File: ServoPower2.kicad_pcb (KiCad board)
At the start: 2 copper layers, 26 x 57.2 mm, 16 parts, among them J1 Conn_01x03, J10 Conn_01x03, J11 Conn_01x03, J12 Conn_01x03, J13 Conn_01x02, J14 Conn_01x02, J15 Conn_01x02, J2 Conn_01x03, J3 Conn_01x03, J4 Conn_01x03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

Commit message: pdb
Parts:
- removed pi1: pi, Connector_PinSocket_2.54mm:PinSocket_2x20_P2.54mm_Vertical
- added U1: Teensy4.0, teensy:Teensy40, F.Cu at (143.5, 82.5)
- moved J12 5.24 mm to (157.5, 104.1)
- moved J11 4.02 mm to (157.5, 101.6)
- moved J9 4.02 mm to (157.5, 94.0)
- moved J6 2.84 mm to (157.5, 83.8)
- moved J8 2.84 mm to (157.5, 91.4)
- moved J10 2.84 mm to (157.5, 99.1)
- moved J3 1.80 mm to (157.5, 73.7)
- moved J1 1.80 mm to (157.5, 68.6)
- moved J5 1.80 mm to (157.5, 81.3)
- moved J7 1.80 mm to (157.5, 88.9)
- moved J14 1.27 mm to (152.4, 63.5)
- moved J13 1.27 mm to (157.5, 114.3)
- moved J2 1.27 mm to (157.5, 71.1)
- moved J4 1.27 mm to (157.5, 78.7)
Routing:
- net +5V: track 4.86 -> 18.6 mm
- net /S41: track 23.8 -> 11.0 mm
- net /S33: track 19.0 -> 9.94 mm
- net /S43: track 24.2 -> 32.0 mm
- net /S32: track 16.6 -> 9.94 mm
- net /S31: track 17.1 -> 10.6 mm
- net /S22: track 13.5 -> 8.89 mm
- net /S21: track 13.0 -> 8.89 mm
- net /S23: track 11.5 -> 8.89 mm
- net /S13: track 8.89 -> 10.6 mm
- net /S42: track 26.2 -> 25.2 mm
- net /S12: track 9.42 -> 9.94 mm
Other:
- board size 26 x 57.2 mm -> 40.6 x 57.8 mm
- net class Power: trace_width 1 -> 0.8
- board text added: "Pupper PDB v0.3 Feb ‘20"
- board text removed: "Pupper PDB v0.2 Oct ‘19"

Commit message: clean up
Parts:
- J13: footprint Connector_AMASS:AMASS_XT30U-M_1x02_P5.0mm_Vertical -> Connector_AMASS:AMASS_XT60-M_1x02_P7.20mm_Vertical
- moved U1 29.3 mm to (172.7, 85.1)
- moved J13 5.12 mm to (161.9, 111.8)
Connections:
- U1 pad 1: Net-(U1-Pad1) -> GND
- U1 pad 12: Net-(U1-Pad12) -> (no net)
- U1 pad 13: Net-(U1-Pad13) -> (no net)
- U1 pad 14: Net-(U1-Pad14) -> (no net)
- U1 pad 15: Net-(U1-Pad15) -> (no net)
- U1 pad 16: Net-(U1-Pad16) -> (no net)
- U1 pad 17: Net-(U1-Pad17) -> GND
- U1 pad 18: Net-(U1-Pad18) -> (no net)
- U1 pad 19: Net-(U1-Pad19) -> (no net)
- U1 pad 20: Net-(U1-Pad20) -> (no net)
- U1 pad 23: Net-(U1-Pad23) -> (no net)
- U1 pad 24: Net-(U1-Pad24) -> (no net)
- U1 pad 25: Net-(U1-Pad25) -> (no net)
- U1 pad 26: Net-(U1-Pad26) -> (no net)
- U1 pad 27: Net-(U1-Pad27) -> (no net)
- U1 pad 28: Net-(U1-Pad28) -> (no net)
- U1 pad 29: Net-(U1-Pad29) -> (no net)
- U1 pad 30: Net-(U1-Pad30) -> (no net)
- U1 pad 31: Net-(U1-Pad31) -> (no net)
- U1 pad 34: Net-(U1-Pad34) -> (no net)
- U1 pad 35: Net-(U1-Pad35) -> (no net)
- U1 pad 36: Net-(U1-Pad36) -> (no net)
- U1 pad 37: Net-(U1-Pad37) -> (no net)
- U1 pad 38: Net-(U1-Pad38) -> (no net)
- U1 pad 39: Net-(U1-Pad39) -> (no net)
- U1 pad 40: Net-(U1-Pad40) -> (no net)
- U1 pad 41: Net-(U1-Pad41) -> (no net)
- U1 pad 42: Net-(U1-Pad42) -> (no net)
- U1 pad 43: Net-(U1-Pad43) -> (no net)
- U1 pad 44: Net-(U1-Pad44) -> (no net)
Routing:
- net /S31: track 10.6 -> 8.67 mm
- net /S13: track 10.6 -> 8.67 mm
- net /S43: track 32.0 -> 30.7 mm
- net /S33: track 9.94 -> 8.67 mm
- net /S32: track 9.94 -> 8.67 mm
- net /S23: track 8.89 -> 7.62 mm
- net /S22: track 8.89 -> 7.62 mm
- net /S21: track 8.89 -> 7.62 mm
- net +5V: track 18.6 -> 17.3 mm
- net /S11: track 9.94 -> 8.67 mm
- net /S41: track 11.0 -> 9.72 mm
- net /S12: track 9.94 -> 8.81 mm
- net /S42: track 25.2 -> 24.3 mm
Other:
- board text added: "Vbat"
- board text removed: "Unregulated Vbat"

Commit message: pcb
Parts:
- added U2: IMUBN, Sparkfun:IMUBN, F.Cu at (198.1, 85.1)
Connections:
- U1 pad 12: (no net) -> Net-(U1-Pad12)
- U1 pad 13: (no net) -> Net-(U1-Pad13)
- U1 pad 14: (no net) -> Net-(U1-Pad14)
- U1 pad 15: (no net) -> Net-(U1-Pad15)
- U1 pad 16: (no net) -> Net-(U1-Pad16)
- U1 pad 18: (no net) -> Net-(U1-Pad18)
- U1 pad 19: (no net) -> Net-(U1-Pad19)
- U1 pad 20: (no net) -> Net-(U1-Pad20)
- U1 pad 23: (no net) -> Net-(U1-Pad23)
- U1 pad 24: (no net) -> /INT
- U1 pad 25: (no net) -> /SDA
- U1 pad 26: (no net) -> /SCL
- U1 pad 27: (no net) -> Net-(U1-Pad27)
- U1 pad 28: (no net) -> Net-(U1-Pad28)
- U1 pad 29: (no net) -> Net-(U1-Pad29)
- U1 pad 30: (no net) -> Net-(U1-Pad30)
- U1 pad 31: (no net) -> Net-(U1-Pad31)
- U1 pad 34: (no net) -> Net-(U1-Pad34)
- U1 pad 35: (no net) -> Net-(U1-Pad35)
- U1 pad 36: (no net) -> Net-(U1-Pad36)
- U1 pad 37: (no net) -> Net-(U1-Pad37)
- U1 pad 38: (no net) -> Net-(U1-Pad38)
- U1 pad 39: (no net) -> Net-(U1-Pad39)
- U1 pad 40: (no net) -> Net-(U1-Pad40)
- U1 pad 41: (no net) -> Net-(U1-Pad41)
- U1 pad 42: (no net) -> Net-(U1-Pad42)
- U1 pad 43: (no net) -> Net-(U1-Pad43)
- U1 pad 44: (no net) -> Net-(U1-Pad44)
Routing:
- net GND: track 0.00 -> 12.8 mm
- net /SCL: track 0.00 -> 11.4 mm
- net /SDA: track 0.00 -> 7.40 mm
- net /INT: track 0.00 -> 7.40 mm
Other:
- board size 40.6 x 57.8 mm -> 67.9 x 57.8 mm

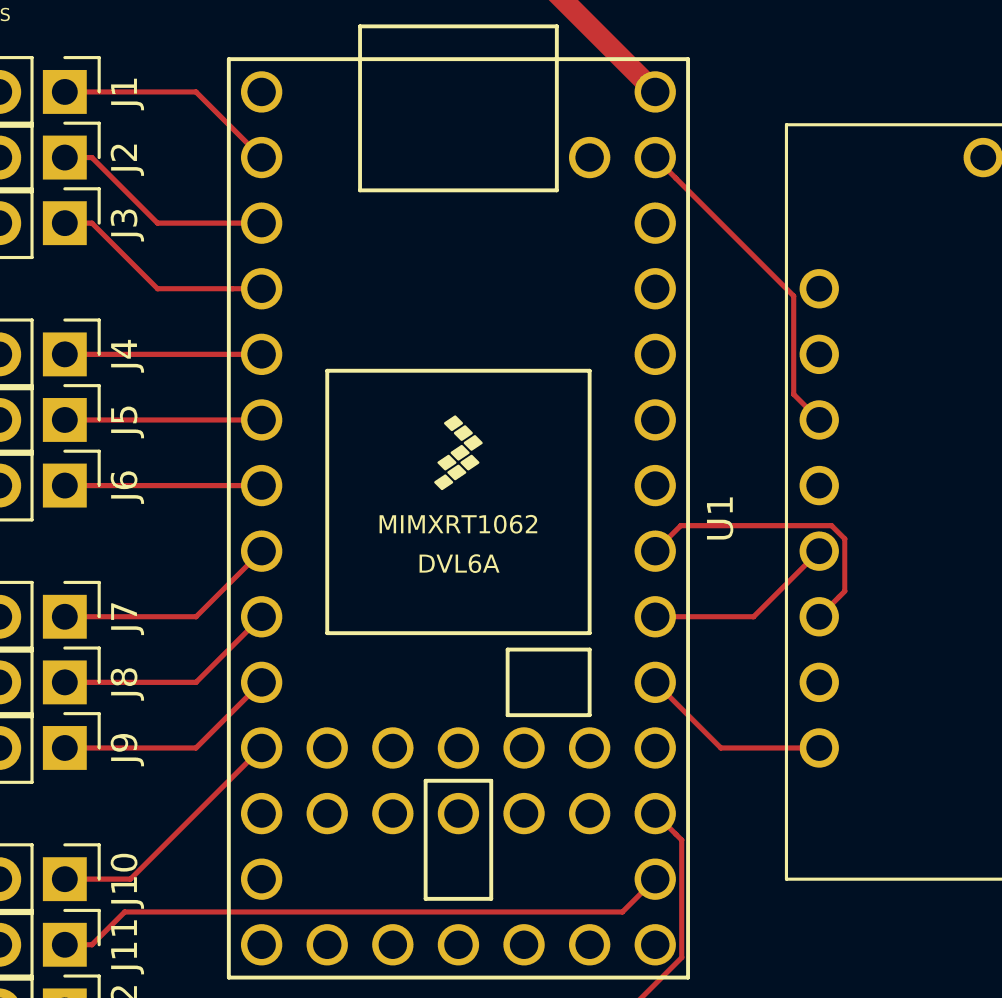
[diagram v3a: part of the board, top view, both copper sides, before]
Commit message: added 3v3
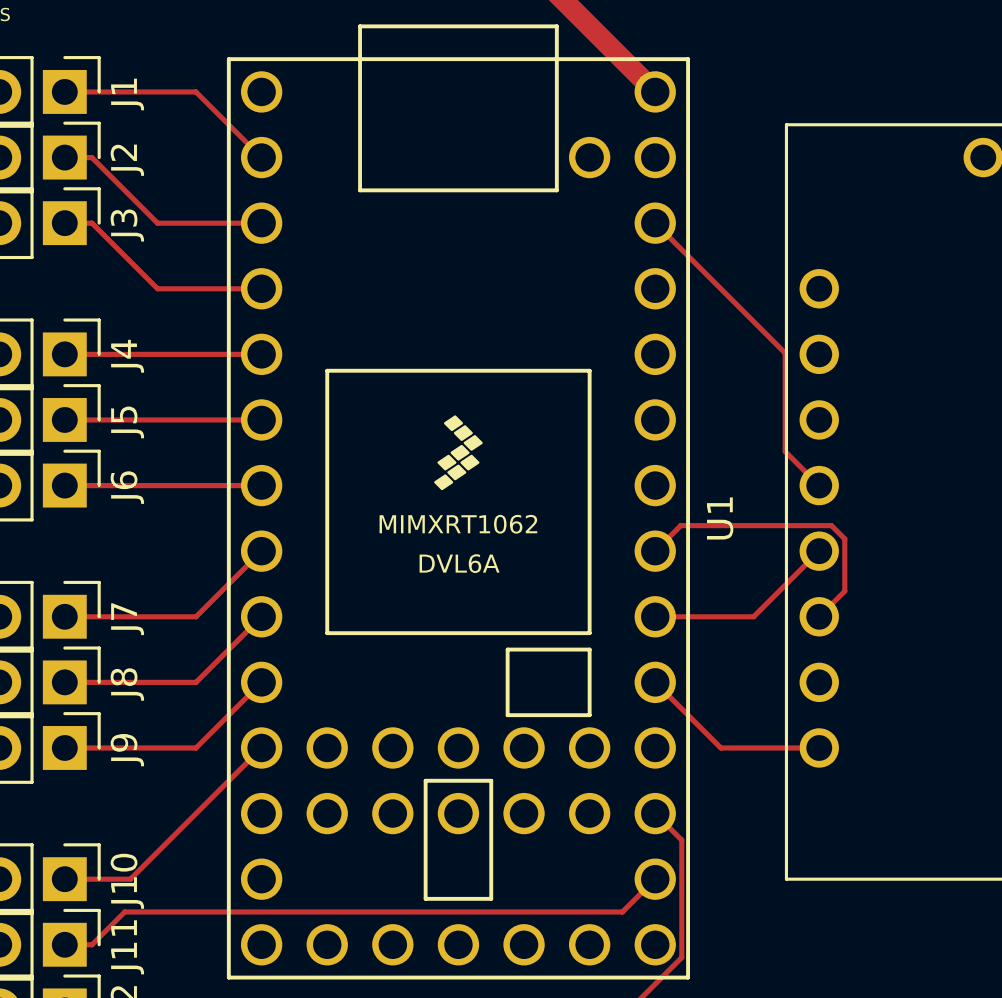
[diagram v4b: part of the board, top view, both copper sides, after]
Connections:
- U1 pad 31: Net-(U1-Pad31) -> +3V3
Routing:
- net +3V3: track 0.00 -> 12.8 mm
- net GND: track 12.8 -> 0.00 mm

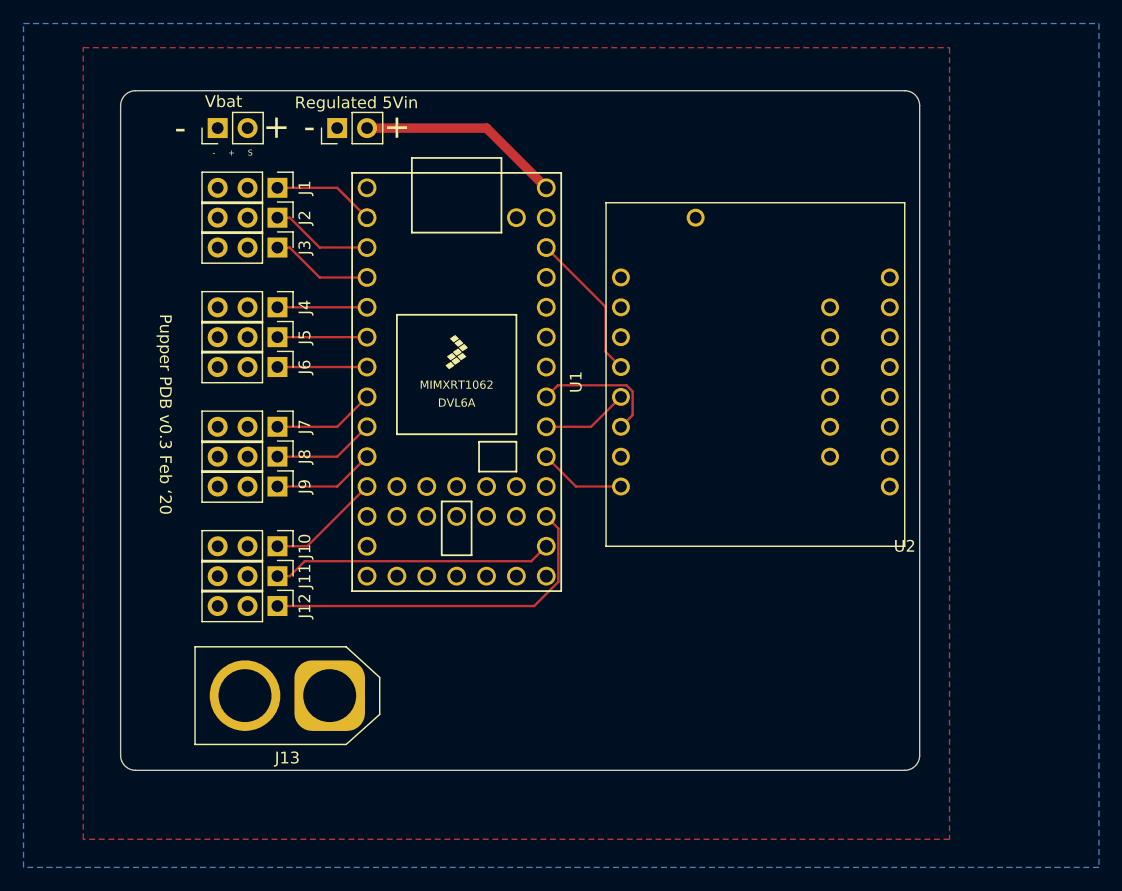
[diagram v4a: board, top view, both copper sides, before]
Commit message: added local dependency to imu symbol and footprint
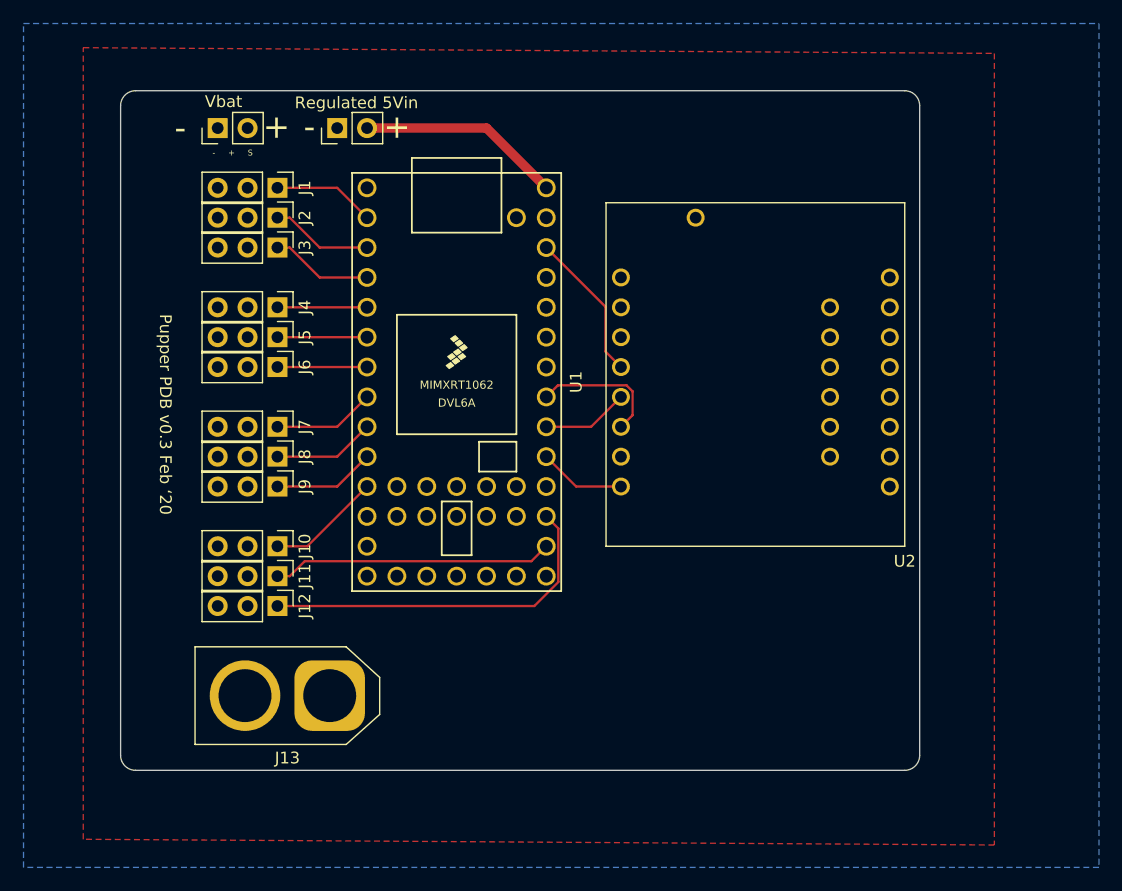
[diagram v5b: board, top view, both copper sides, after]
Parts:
- U2: footprint Sparkfun:IMUBN -> IMU_library:IMUBN
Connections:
- U1 pad 12: Net-(U1-Pad12) -> (no net)
- U1 pad 13: Net-(U1-Pad13) -> (no net)
- U1 pad 14: Net-(U1-Pad14) -> (no net)
- U1 pad 15: Net-(U1-Pad15) -> (no net)
- U1 pad 16: Net-(U1-Pad16) -> (no net)
- U1 pad 18: Net-(U1-Pad18) -> (no net)
- U1 pad 19: Net-(U1-Pad19) -> (no net)
- U1 pad 20: Net-(U1-Pad20) -> (no net)
- U1 pad 23: Net-(U1-Pad23) -> (no net)
- U1 pad 27: Net-(U1-Pad27) -> (no net)
- U1 pad 28: Net-(U1-Pad28) -> (no net)
- U1 pad 29: Net-(U1-Pad29) -> (no net)
- U1 pad 30: Net-(U1-Pad30) -> (no net)
- U1 pad 31: +3V3 -> (no net)
- U1 pad 34: Net-(U1-Pad34) -> (no net)
- U1 pad 35: Net-(U1-Pad35) -> (no net)
- U1 pad 36: Net-(U1-Pad36) -> (no net)
- U1 pad 37: Net-(U1-Pad37) -> (no net)
- U1 pad 38: Net-(U1-Pad38) -> (no net)
- U1 pad 39: Net-(U1-Pad39) -> (no net)
- U1 pad 40: Net-(U1-Pad40) -> (no net)
- U1 pad 41: Net-(U1-Pad41) -> (no net)
- U1 pad 42: Net-(U1-Pad42) -> (no net)
- U1 pad 43: Net-(U1-Pad43) -> (no net)
- U1 pad 44: Net-(U1-Pad44) -> (no net)
- U2 pad 1: Net-(U2-Pad1) -> (no net)
- U2 pad 10: Net-(U2-Pad10) -> (no net)
- U2 pad 11: Net-(U2-Pad11) -> (no net)
- U2 pad 12: Net-(U2-Pad12) -> (no net)
- U2 pad 13: Net-(U2-Pad13) -> (no net)
- U2 pad 14: Net-(U2-Pad14) -> (no net)
- U2 pad 15: Net-(U2-Pad15) -> (no net)
- U2 pad 16: Net-(U2-Pad16) -> (no net)
- U2 pad 2: Net-(U2-Pad2) -> (no net)
- U2 pad 4: +3V3 -> (no net)
- U2 pad 7: Net-(U2-Pad7) -> (no net)
- U2 pad 9: Net-(U2-Pad9) -> (no net)
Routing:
- net +3V3: track 12.8 -> 0.00 mm
- net (no net): track 0.00 -> 12.8 mm
